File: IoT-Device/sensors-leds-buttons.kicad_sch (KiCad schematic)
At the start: 13 parts, among them SW3 B1, SW4 B2

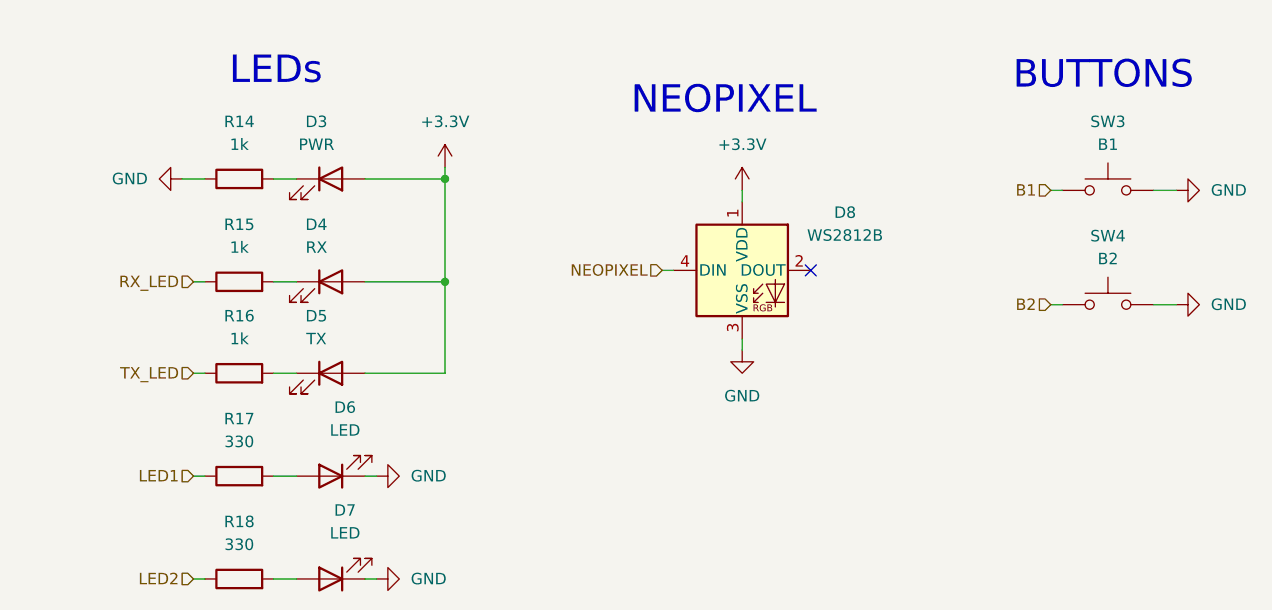
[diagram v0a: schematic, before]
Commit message: connect USB-C port's CC1 and CC2 to STM32's CC1 and CC2 pins
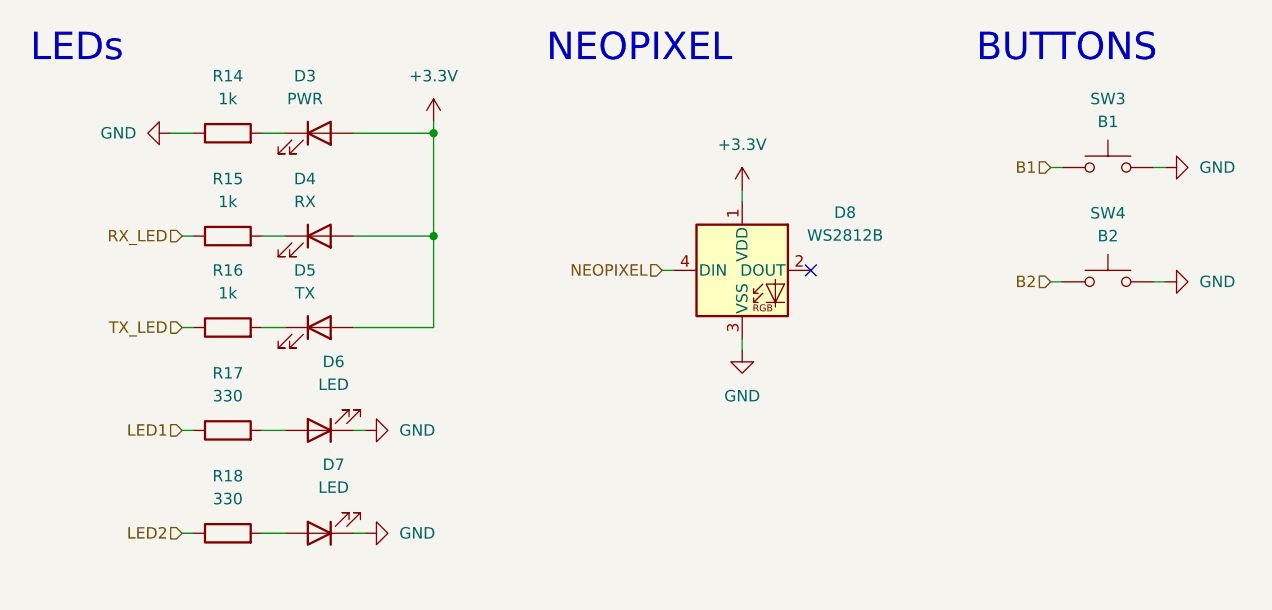
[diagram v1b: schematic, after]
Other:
- moved on the sheet: D3, D4, D5, D6, D7, R14, R15, R16, R17, R18, SW3, SW4

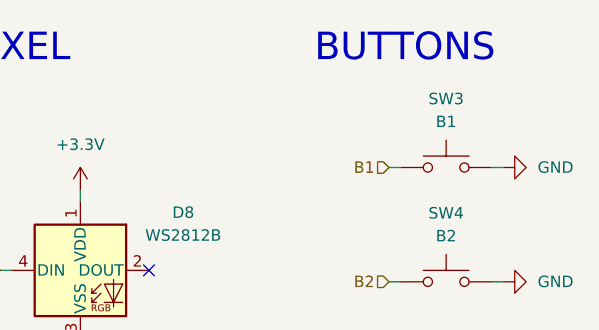
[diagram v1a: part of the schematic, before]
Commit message: add microSD card slot
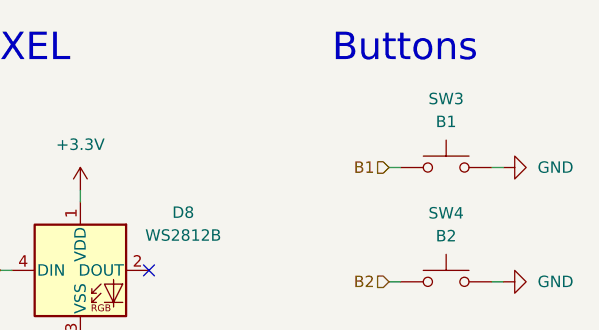
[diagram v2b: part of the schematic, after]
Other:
- note added: "Buttons"
- note removed: "BUTTONS"
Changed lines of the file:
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@@
 		)
 	)
-	(text "BUTTONS"
+	(text "Buttons"
 		(exclude_from_sim no)
 		(at 128.778 16.002 0)

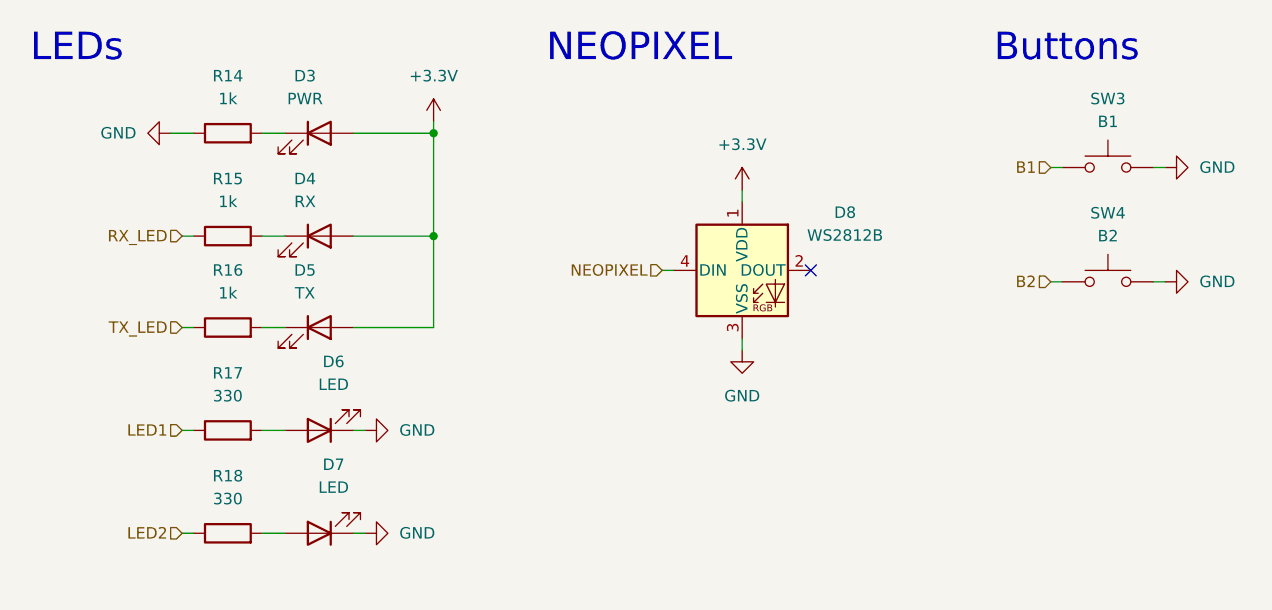
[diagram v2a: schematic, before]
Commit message: fix STM32<->ESP32-C3 UART communication, update labels on shcematics
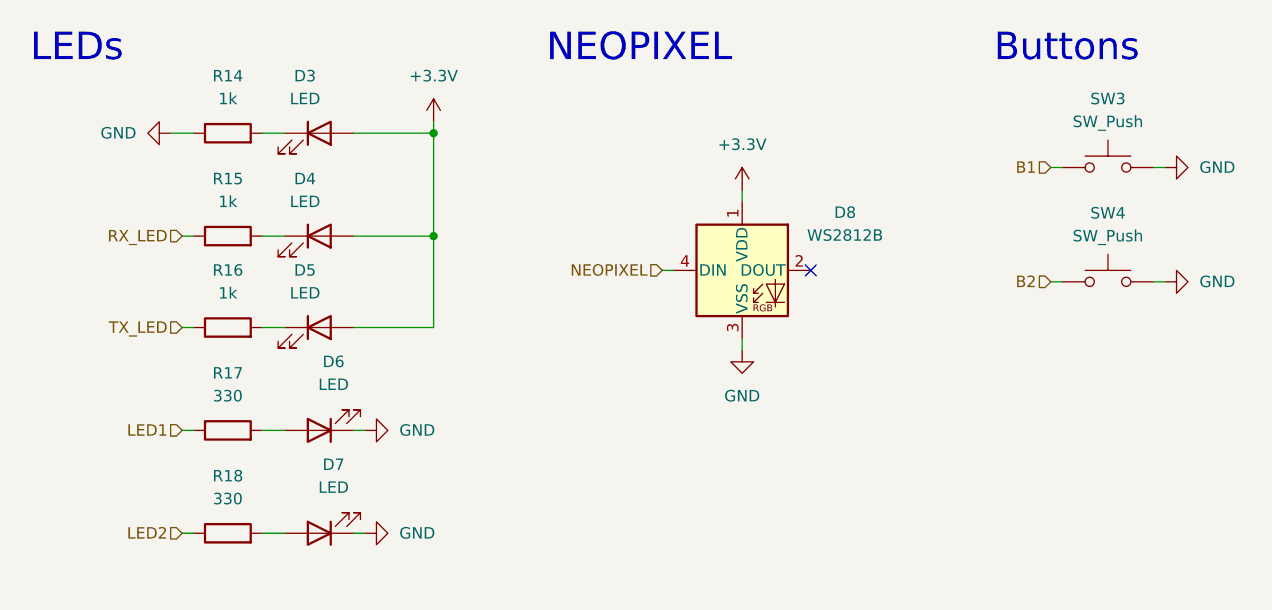
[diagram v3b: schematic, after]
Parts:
- D3: value PWR -> LED
- D4: value RX -> LED
- D5: value TX -> LED
- SW3: value B1 -> SW_Push
- SW4: value B2 -> SW_Push
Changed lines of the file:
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@@
 			)
 		)
-		(property "Value" "B1"
+		(property "Value" "SW_Push"
 			(at 133.35 24.13 0)
 			(effects
@@
 			)
 		)
-		(property "Value" "PWR"
+		(property "Value" "LED"
 			(at 44.1325 21.59 0)
 			(effects
@@
 			)
 		)
-		(property "Value" "TX"
+		(property "Value" "LED"
 			(at 44.1325 43.18 0)
 			(effects
@@
 			)
 		)
-		(property "Value" "B2"
+		(property "Value" "SW_Push"
 			(at 133.35 36.83 0)
 			(effects
@@
 			)
 		)
-		(property "Value" "RX"
+		(property "Value" "LED"
 			(at 44.1325 33.02 0)
 			(effects
